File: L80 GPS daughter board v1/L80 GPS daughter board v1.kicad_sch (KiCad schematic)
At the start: 14 parts, among them J1 Conn_01x06_Socket, J2 THD2528-11SD-GF, SW1 SW_Push, U1 AP2112K-3.3, U2 L80-R, U3 MCP73831-2-OT

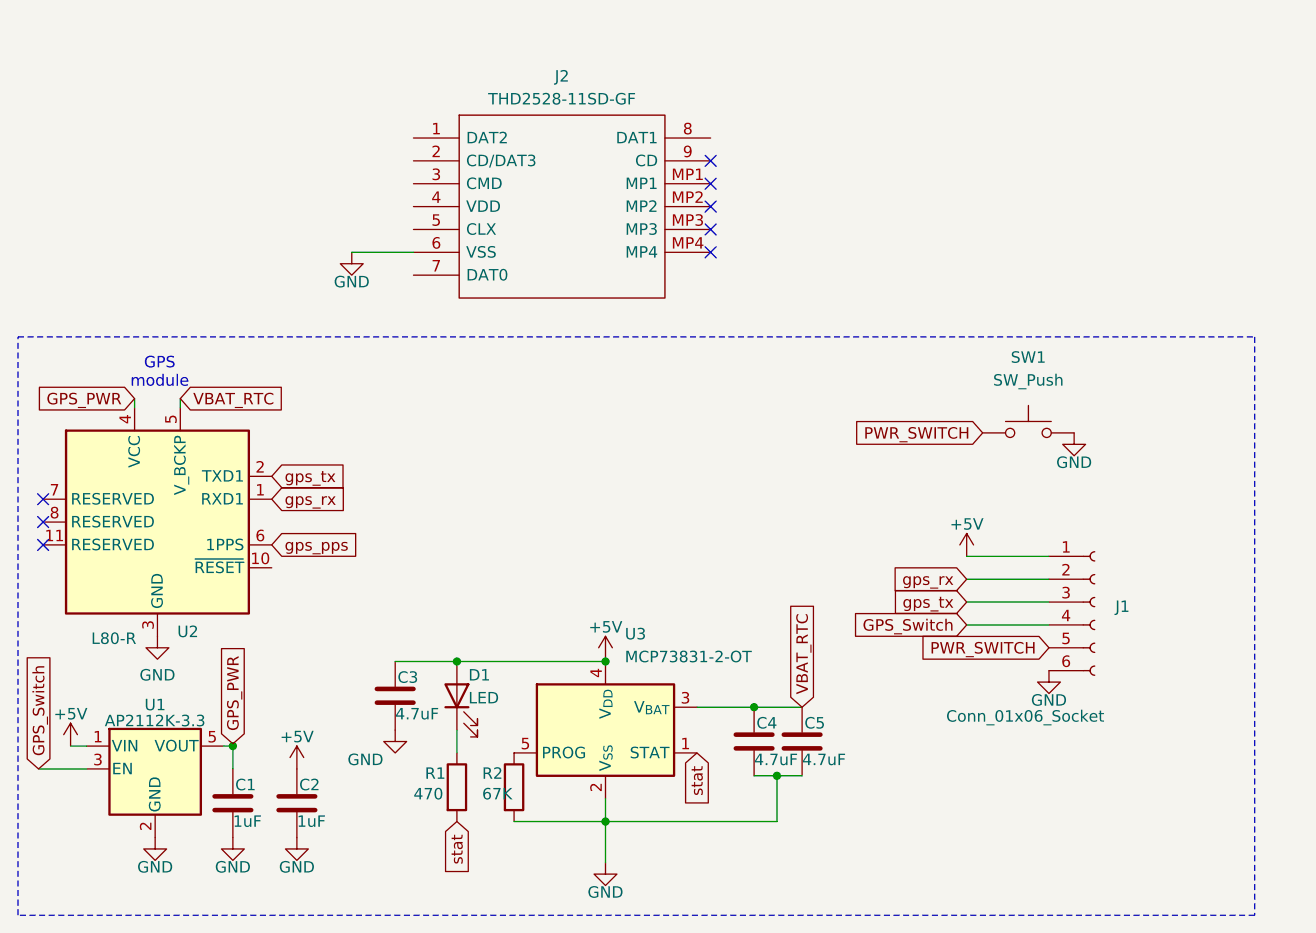
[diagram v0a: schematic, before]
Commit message: modefied gps board to handle sdcard operations and power input
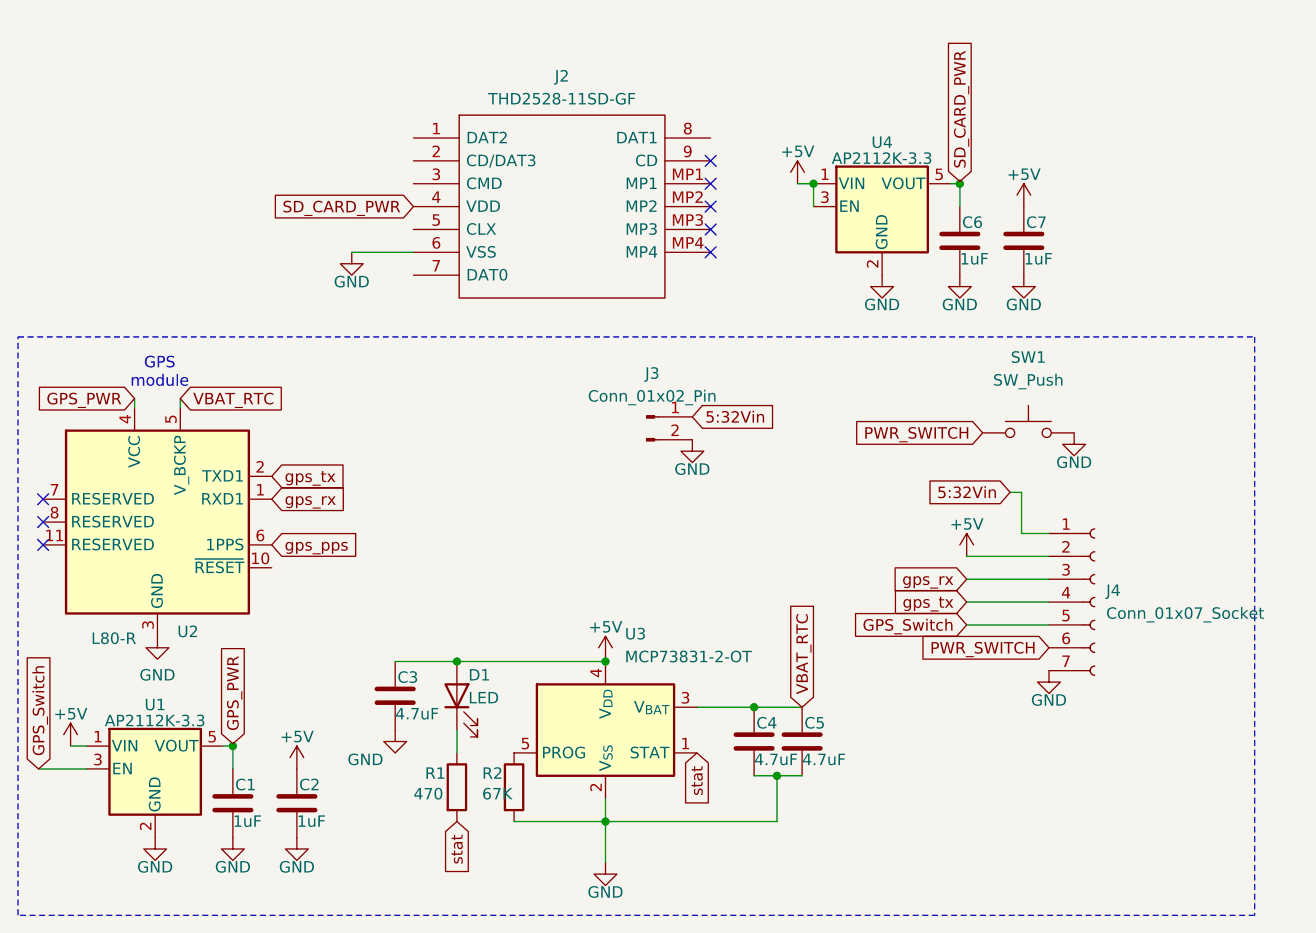
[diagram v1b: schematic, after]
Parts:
- removed J1: Conn_01x06_Socket, Connector_PinHeader_2.54mm:PinHeader_1x06_P2.54mm_Vertical, symbol Connector:Conn_01x06_Socket
- added C6, C7: 1uF, Capacitor_SMD:C_0603_1608Metric, symbol Device:C
- added J3: Conn_01x02_Pin, Connector_PinHeader_2.54mm:PinHeader_1x02_P2.54mm_Vertical, symbol Connector:Conn_01x02_Pin
- added J4: Conn_01x07_Socket, Connector_PinSocket_2.54mm:PinSocket_1x07_P2.54mm_Vertical, symbol Connector:Conn_01x07_Socket
- added U4: AP2112K-3.3, Package_TO_SOT_SMD:SOT-23-5, symbol Regulator_Linear:AP2112K-3.3
- J2: footprint THD252811SDGF -> KiCad:THD252811SDGF
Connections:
- net +5V: now also C7.1, J4.2 (Pin_2), U4.1 (VIN), U4.3 (EN)
- net GND: now also C6.2, C7.2, J3.2 (Pin_2), J4.7 (Pin_7), U4.2 (GND)
- net GPS_Switch: now also J4.5 (Pin_5)
- net PWR_SWITCH: now also J4.6 (Pin_6)
- net gps_rx: now also J4.3 (Pin_3)
- net gps_tx: now also J4.4 (Pin_4)
- net SD_CARD_PWR: now reaches J2.4 (VDD)
- net SD_CARD_PWR: now also C6.1, U4.5 (VOUT)
- new net 5:32Vin: J3.1 (Pin_1), J4.1 (Pin_1)

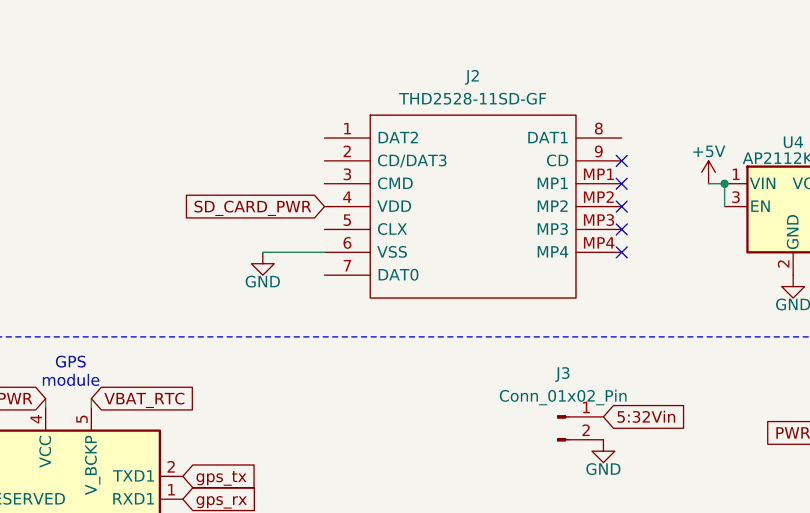
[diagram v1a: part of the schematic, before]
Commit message: added SD card pinout
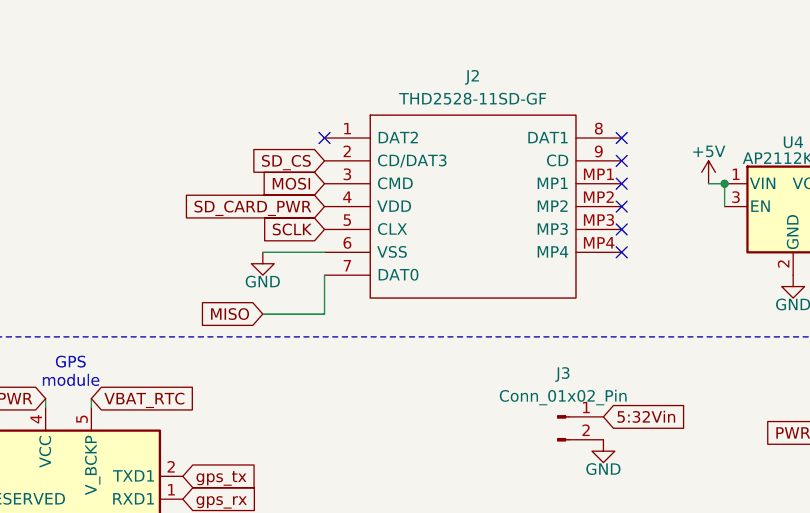
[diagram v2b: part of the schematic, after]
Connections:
- net SD_CS: now reaches J2.2 (CD/DAT3)
- net MOSI: now reaches J2.3 (CMD)
- net SCLK: now reaches J2.5 (CLX)
- net MISO: now reaches J2.7 (DAT0)
- no-connect marks 8 -> 10
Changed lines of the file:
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@@
+	)
+	(no_connect
+		(at 118.618 52.578)
+	)
+	(no_connect
+		(at 151.638 52.578)
 	)
 	(no_connect
@@
 	(wire
 		(pts
+			(xy 111.76 72.136) (xy 118.618 72.136)
+		)
+		(stroke
+			(width 0)
+			(type default)
+		)
+	)
+	(wire
+		(pts
 			(xy 139.954 128.524) (xy 139.954 125.984)
 		)
@@
 		)
 	)
+	(wire
+		(pts
+			(xy 118.618 72.136) (xy 118.618 67.818)
+		)
+		(stroke
+			(width 0)
+			(type default)
+		)
+	)
 	(global_label "SD_CARD_PWR"
 		(shape input)
@@
 		)
 	)
+	(global_label "SD_CS"
+		(shape input)
+		(at 118.618 55.118 180)
+		(fields_autoplaced yes)
+		(effects
+			(font
+				(size 1.27 1.27)
+			)
+			(justify right)
+		)
+		(property "Intersheetrefs" "${INTERSHEET_REFS}"
+			(at 109.7062 55.118 0)
+			(effects
+				(font
+					(size 1.27 1.27)
+				)
+				(justify right)
+				(hide yes)
+			)
+		)
+	)
 	(global_label "GPS_Switch"
 		(shape input)
@@
 		)
 	)
+	(global_label "MOSI"
+		(shape input)
+		(at 118.618 57.658 180)
+		(fields_autoplaced yes)
+		(effects
+			(font
+				(size 1.27 1.27)
+			)
+			(justify right)
+		)
+		(property "Intersheetrefs" "${INTERSHEET_REFS}"
+			(at 111.0366 57.658 0)
+			(effects
+				(font
+					(size 1.27 1.27)
+				)
+				(justify right)
+				(hide yes)
+			)
+		)
+	)
 	(global_label "PWR_SWITCH"
 		(shape input)
@@
 		)
 	)
+	(global_label "MISO"
+		(shape input)
+		(at 111.76 72.136 180)
+		(fields_autoplaced yes)
+		(effects
+			(font
+				(size 1.27 1.27)
+			)
+			(justify right)
+		)
+		(property "Intersheetrefs" "${INTERSHEET_REFS}"
+			(at 104.1786 72.136 0)
+			(effects
+				(font
+					(size 1.27 1.27)
+				)
+				(justify right)
+				(hide yes)
+			)
+		)
+	)
 	(global_label "gps_tx"
 		(shape input)
@@
 				(hide yes)
 			)
+		)
+	)
+	(global_label "SCLK"
+		(shape input)
+		(at 118.618 62.738 180)
+		(fields_autoplaced yes)
+		(effects
+			(font
+				(size 1.27 1.27)
+			)
+			(justify right)
+		)
+		(property "Intersheetrefs" "${INTERSHEET_REFS}"
+			(at 110.8552 62.738 0)
+			(effects
+				(font
+					(size 1.27 1.27)
+				)
+				(justify right)
+				(hide yes)
+			)

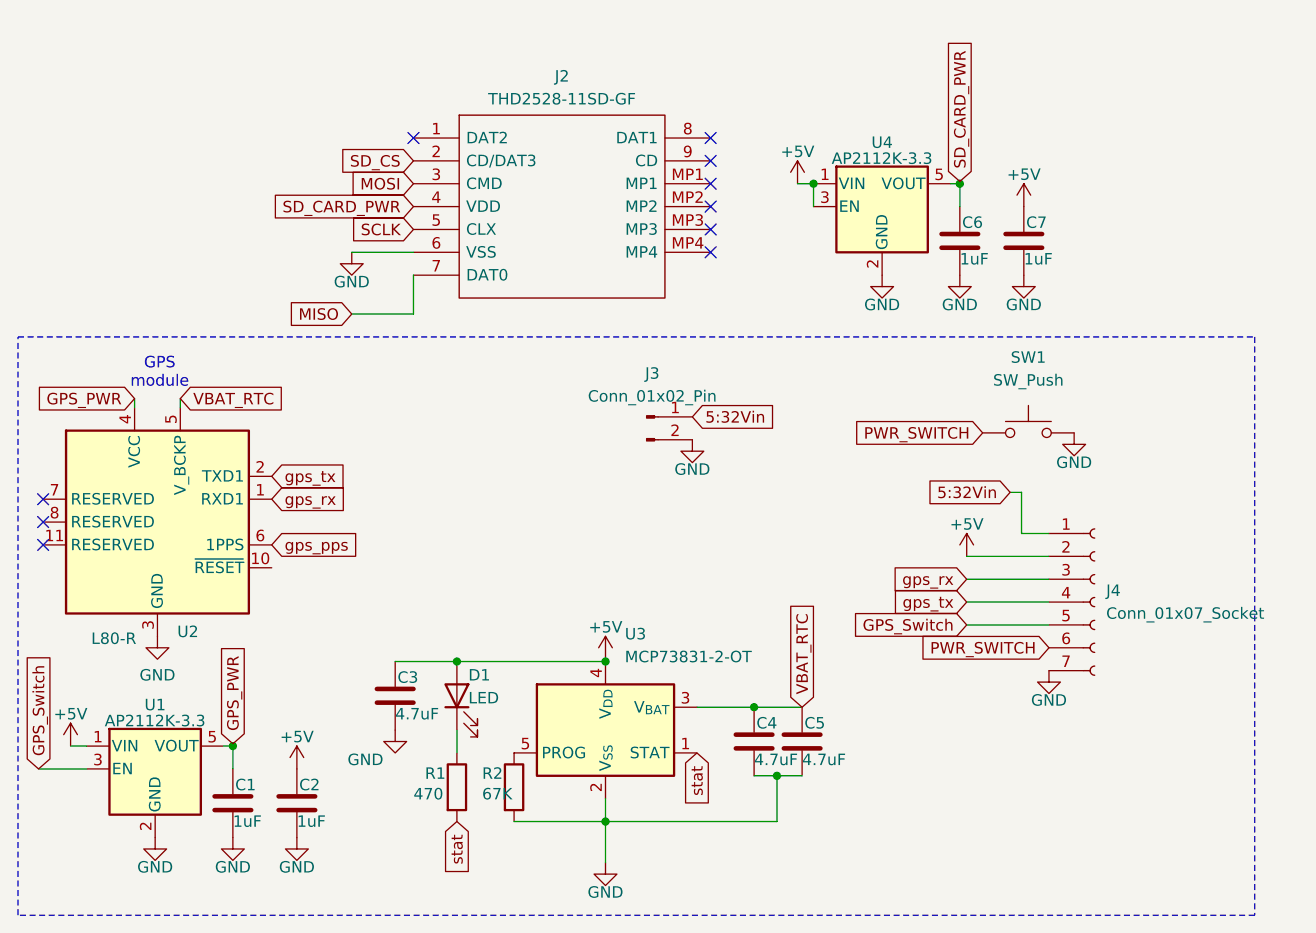
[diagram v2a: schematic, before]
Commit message: cleaned up sd card routing and added appropriate connectors
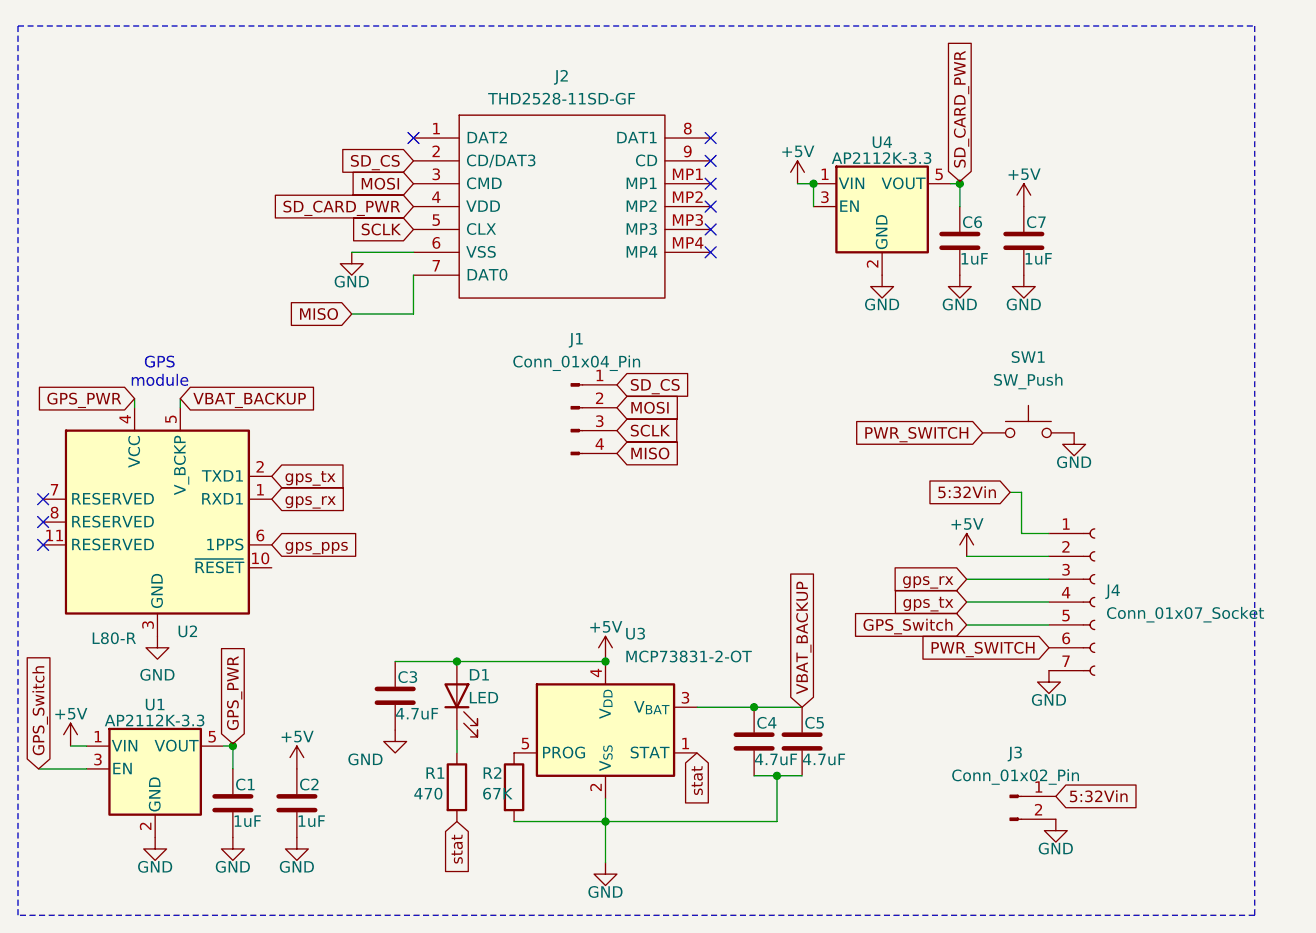
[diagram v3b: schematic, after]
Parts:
- added J1: Conn_01x04_Pin, Connector_PinHeader_2.00mm:PinHeader_1x04_P2.00mm_Vertical_SMD_Pin1Left, symbol Connector:Conn_01x04_Pin
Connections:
- net MISO: now also J1.4 (Pin_4)
- net MOSI: now also J1.2 (Pin_2)
- net SCLK: now also J1.3 (Pin_3)
- net SD_CS: now also J1.1 (Pin_1)
- net VBAT_RTC renamed VBAT_BACKUP
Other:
- moved on the sheet: J3
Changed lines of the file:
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@@
 	(paper "A4")
 	(rectangle
-		(start 74.676 74.676)
+		(start 74.676 40.132)
 		(end 212.09 138.938)
 		(stroke
@@
 		)
 	)
-	(global_label "VBAT_RTC"
+	(global_label "VBAT_BACKUP"
 		(shape input)
 		(at 161.798 115.824 90)
@@
 		)
 		(property "Intersheetrefs" "${INTERSHEET_REFS}"
-			(at 161.798 103.9488 90)
+			(at 161.798 99.9573 90)
 			(effects
 				(font
@@
 		)
 	)
+	(global_label "SCLK"
+		(shape input)
+		(at 141.224 85.09 0)
+		(fields_autoplaced yes)
+		(effects
+			(font
+				(size 1.27 1.27)
+			)
+			(justify left)
+		)
+		(property "Intersheetrefs" "${INTERSHEET_REFS}"
+			(at 148.9868 85.09 0)
+			(effects
+				(font
+					(size 1.27 1.27)
+				)
+				(justify left)
+				(hide yes)
+			)
+		)
+	)
 	(global_label "5:32Vin"
 		(shape input)
@@
 		)
 	)
-	(global_label "VBAT_RTC"
+	(global_label "MOSI"
+		(shape input)
+		(at 141.224 82.55 0)
+		(fields_autoplaced yes)
+		(effects
+			(font
+				(size 1.27 1.27)
+			)
+			(justify left)
+		)
+		(property "Intersheetrefs" "${INTERSHEET_REFS}"
+			(at 148.8054 82.55 0)
+			(effects
+				(font
+					(size 1.27 1.27)
+				)
+				(justify left)
+				(hide yes)
+			)
+		)
+	)
+	(global_label "SD_CS"
+		(shape input)
+		(at 141.224 80.01 0)
+		(fields_autoplaced yes)
+		(effects
+			(font
+				(size 1.27 1.27)
+			)
+			(justify left)
+		)
+		(property "Intersheetrefs" "${INTERSHEET_REFS}"
+			(at 150.1358 80.01 0)
+			(effects
+				(font
+					(size 1.27 1.27)
+				)
+				(justify left)
+				(hide yes)
+			)
+		)
+	)
+	(global_label "VBAT_BACKUP"
 		(shape input)
 		(at 92.71 81.534 0)
@@
 		)
 		(property "Intersheetrefs" "${INTERSHEET_REFS}"
-			(at 104.5852 81.534 0)
+			(at 108.5767 81.534 0)
 			(effects
 				(font
@@
 	(global_label "5:32Vin"
 		(shape input)
-		(at 149.606 83.566 0)
+		(at 189.992 125.73 0)
 		(fields_autoplaced yes)
 		(effects
@@
 		)
 		(property "Intersheetrefs" "${INTERSHEET_REFS}"
-			(at 159.6669 83.566 0)
+			(at 200.0529 125.73 0)
 			(effects
 				(font
@@
 				(justify right)
 				(hide yes)
+			)
+		)
+	)
+	(global_label "MISO"
+		(shape input)
+		(at 141.224 87.63 0)
+		(fields_autoplaced yes)
+		(effects
+			(font
+				(size 1.27 1.27)
+			)
+			(justify left)
+		)
+		(property "Intersheetrefs" "${INTERSHEET_REFS}"
+			(at 148.8054 87.63 0)
+			(effects
+				(font
+					(size 1.27 1.27)
+				)
+				(justify left)
+				(hide yes)
+			)
+		)
+	)
+	(symbol
+		(lib_id "Connector:Conn_01x04_Pin")
+		(at 136.144 82.55 0)
+		(unit 1)
+		(exclude_from_sim no)
+		(in_bom yes)
+		(on_board yes)
+		(dnp no)
+		(fields_autoplaced yes)
+		(property "Reference" "J1"
+			(at 136.779 74.93 0)
+			(effects
+				(font
+					(size 1.27 1.27)
+				)
+			)
+		)
+		(property "Value" "Conn_01x04_Pin"
+			(at 136.779 77.47 0)
+			(effects
+				(font
+					(size 1.27 1.27)
+				)
+			)
+		)
+		(property "Footprint" "Connector_PinHeader_2.00mm:PinHeader_1x04_P2.00mm_Vertical_SMD_Pin1Left"
+			(at 136.144 82.55 0)
+			(effects
+				(font
+					(size 1.27 1.27)
+				)
+				(hide yes)
+			)
+		)
+		(property "Datasheet" "~"
+			(at 136.144 82.55 0)
+			(effects
+				(font
+					(size 1.27 1.27)
+				)
+				(hide yes)
+			)
+		)
+		(property "Description" "Generic connector, single row, 01x04, script generated"
+			(at 136.144 82.55 0)
+			(effects
+				(font
+					(size 1.27 1.27)
+				)
+				(hide yes)
+			)
+		)
+		(pin "4"
+		)
+		(pin "3"
+		)
+		(pin "1"
+		)
+		(pin "2"
+		)
+		(instances
+			(project ""
+				(path "/d19b7dbb-d08f-4a81-9071-b9150d5b9101"
+					(reference "J1")
+					(unit 1)
+				)
 			)
 		)
@@
 	(symbol
 		(lib_id "Connector:Conn_01x02_Pin")
-		(at 144.526 83.566 0)
+		(at 184.912 125.73 0)
 		(unit 1)
 		(exclude_from_sim no)
@@
 		(fields_autoplaced yes)
 		(property "Reference" "J3"
-			(at 145.161 78.74 0)
+			(at 185.547 120.904 0)
 			(effects
 				(font
@@
 		)
 		(property "Value" "Conn_01x02_Pin"
-			(at 145.161 81.28 0)
+			(at 185.547 123.444 0)
 			(effects
 				(font
@@
 		)
 		(property "Footprint" "Connector_PinHeader_2.54mm:PinHeader_1x02_P2.54mm_Vertical"
-			(at 144.526 83.566 0)
+			(at 184.912 125.73 0)
 			(effects
 				(font
@@
 		)
 		(property "Datasheet" "~"
-			(at 144.526 83.566 0)
+			(at 184.912 125.73 0)
 			(effects
 				(font
@@
 		)
 		(property "Description" "Generic connector, single row, 01x02, script generated"
-			(at 144.526 83.566 0)
+			(at 184.912 125.73 0)
 			(effects
 				(font
@@
 	(symbol
 		(lib_id "power:GND")
-		(at 149.606 86.106 0)
+		(at 189.992 128.27 0)
 		(unit 1)
 		(exclude_from_sim no)
@@
 		(dnp no)
 		(property "Reference" "#PWR019"
-			(at 149.606 92.456 0)
+			(at 189.992 134.62 0)
 			(effects
 				(font
@@
 		)
 		(property "Value" "GND"
-			(at 149.606 89.408 0)
+			(at 189.992 131.572 0)
 			(effects
 				(font
@@
 		)
 		(property "Footprint" ""
-			(at 149.606 86.106 0)
+			(at 189.992 128.27 0)
 			(effects
 				(font
@@
 		)
 		(property "Datasheet" ""
-			(at 149.606 86.106 0)
+			(at 189.992 128.27 0)
 			(effects
 				(font
@@
 		)
 		(property "Description" ""
-			(at 149.606 86.106 0)
-			(effects
-				(font
+			(at 189.992 128.27 0)
+			(effects
+				(font
